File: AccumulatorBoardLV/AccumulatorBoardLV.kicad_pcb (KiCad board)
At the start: 4 copper layers, 152.4 x 50.8 mm, 50 parts, among them J1 Contactor 1, J10 To HV Board, J11 IMD Reset, J12 TS Interlock, J13 Temp Reset, J14 To ECU, J15 Charger LV, J16 Charger Interlock, J17 Lid Interlock, J18 From HV Board, J19 Chip 1, J2 BMS Connector 1, J20 Chip 2, J21 Chip 3, J22 Chip 4, J3 BMS Connector 2, J4 BMS TX, J5 BMS RX, J6 Current Sensor, J7 Contactor 2, J8 IMD LV, J9 BMS Reset, U1 DE1A1B-L2-12V, U10 MCP3008, U11 ISO1050, U12 stm_nucleo_FK303K8, U13 MCP3008, U14 MCP3008, U2 LM555N, U3 SN754410, U4 DE1A1B-L2-12V, U5 L78S05CV-DG, U6 DE1A1B-L2-12V, U7 DK1A1B-12V, U8 ADUM4154ARIZ, U9 MCP3008

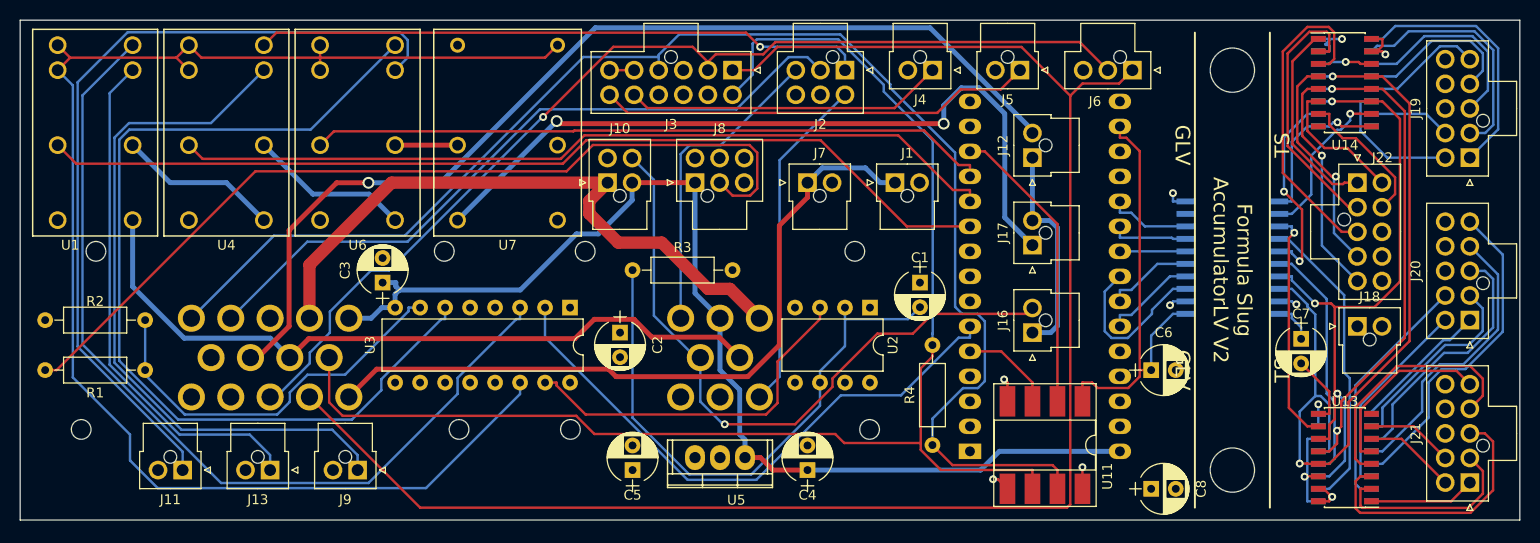
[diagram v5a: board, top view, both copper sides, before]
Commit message: Update DE relay footprint
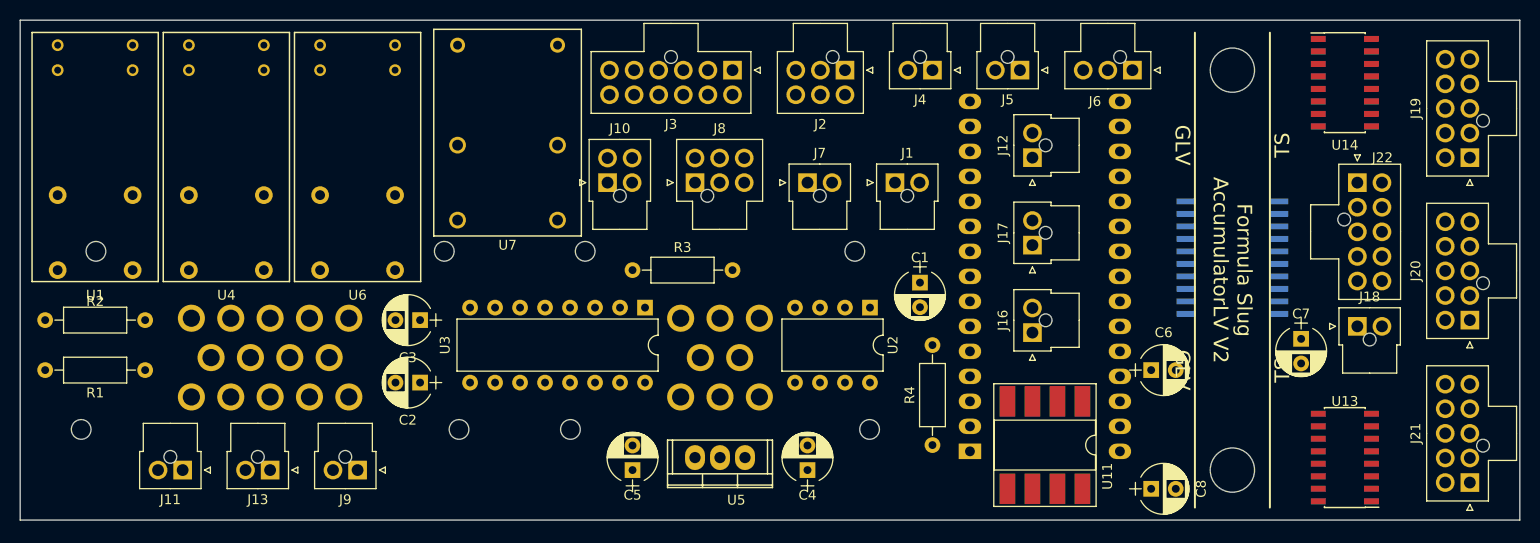
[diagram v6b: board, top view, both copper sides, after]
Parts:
- moved C2 20.9 mm to (80.9, 144.0), turned to 180 degrees
- moved U3 7.62 mm to (103.8, 136.4)
- moved C3 5.39 mm to (80.9, 137.7), turned to 180 degrees
- moved U1 5.08 mm to (44.1, 125.0)
- moved U4 5.08 mm to (57.4, 125.0)
- moved U6 5.08 mm to (70.7, 125.0)
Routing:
- net /5V_BMS: track 168.4 -> 0.00 mm
- net /TIMER_H: track 147.7 -> 0.00 mm
- net /CAN_H: track 146.8 -> 0.00 mm
- net /CAN_L: track 141.6 -> 0.00 mm
- net +12V: track 114.4 -> 0.00 mm
- net /SIG_CURRENT: track 105.2 -> 0.00 mm, vias 1 -> 0
- net /AIRS_ACC_OUT: track 103.7 -> 0.00 mm, vias 1 -> 0
- net /TEMP_FLT_LATCHED: track 98.1 -> 0.00 mm
- net /IMD_FLT_H: track 96.1 -> 0.00 mm
- net /TEMP_FLT_H: track 91.8 -> 0.00 mm
- net /IMD_FLT: track 90.5 -> 0.00 mm
- net /BMS_FLT_LATCHED: track 84.4 -> 0.00 mm
- net /IMD_RESET: track 83.4 -> 0.00 mm
- net /SCLK: track 81.8 -> 0.00 mm, vias 2 -> 0
- net /AIRS_RELAYS_OUT: track 78.1 -> 0.00 mm, vias 2 -> 0
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
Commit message: tweak boards slightly
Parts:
- added C9: CP, Capacitors_THT:C_Disc_D3.0mm_W1.6mm_P2.50mm, F.Cu at (145.7, 140.8)
- C2: value 0.47uF -> 0.1uF; footprint Capacitors_THT:CP_Radial_D5.0mm_P2.50mm -> Capacitors_THT:C_Disc_D3.0mm_W1.6mm_P2.50mm
- C3: value 10uF -> 0.1uF; footprint Capacitors_THT:CP_Radial_D5.0mm_P2.50mm -> Capacitors_THT:C_Disc_D3.0mm_W1.6mm_P2.50mm
- C6: value CP -> 0.1uF; footprint Capacitors_THT:CP_Radial_D5.0mm_P2.50mm -> Capacitors_THT:C_Disc_D3.0mm_W1.6mm_P2.50mm
- C7: value C -> 0.1uF; footprint Capacitors_THT:CP_Radial_D5.0mm_P2.50mm -> Capacitors_THT:C_Disc_D3.0mm_W1.6mm_P2.50mm
- C8: footprint Capacitors_THT:CP_Radial_D5.0mm_P2.50mm -> Capacitors_THT:C_Disc_D3.0mm_W1.6mm_P2.50mm
- moved R4 10.2 mm to (133.0, 140.2), turned to 270 degrees
- moved C8 9.71 mm to (145.7, 156.7), turned to 180 degrees
- moved C6 4.49 mm to (158.4, 139.6), turned to 180 degrees
- moved J16 2.54 mm to (143.1, 136.4)
- moved C7 1.91 mm to (168.5, 139.6), turned to 0 degrees
- moved J17 1.91 mm to (143.1, 128.1)
- moved C3 1.80 mm to (82.2, 136.4), turned to 270 degrees
- moved C2 1.27 mm to (82.2, 144.0), turned to 90 degrees
- moved J12 1.27 mm to (143.1, 119.9)
- moved U11 1.27 mm to (144.4, 149.1)
- moved U7 0.64 mm to (89.8, 119.3)
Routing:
- net /CAN_H: track 0.00 -> 136.6 mm
- net /CAN_L: track 0.00 -> 124.7 mm
- net /AIRS_ACC_OUT: track 0.00 -> 122.2 mm
- net /5V_BMS: track 0.00 -> 117.1 mm
- net /TIMER_H: track 0.00 -> 117.1 mm, vias 0 -> 1
- net /SIG_CURRENT: track 0.00 -> 116.7 mm, vias 0 -> 1
- net +12V: track 0.00 -> 116.5 mm, vias 0 -> 1
- net /TEMP_FLT_LATCHED: track 0.00 -> 101.6 mm, vias 0 -> 1
- net /IMD_FLT: track 0.00 -> 89.2 mm
- net /BMS_FLT_LATCHED: track 0.00 -> 88.3 mm, vias 0 -> 1
- net /AIRS_FINAL: track 0.00 -> 88.1 mm
- net /AIRS_RELAYS_OUT: track 0.00 -> 74.6 mm
- net /AIRS_FINAL_CHARGER: track 0.00 -> 74.2 mm
- net /TEMP_SSO: track 0.00 -> 73.1 mm, vias 0 -> 2
- net /V_L: track 0.00 -> 72.3 mm
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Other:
- net class Power: via_dia 2.4 -> 100

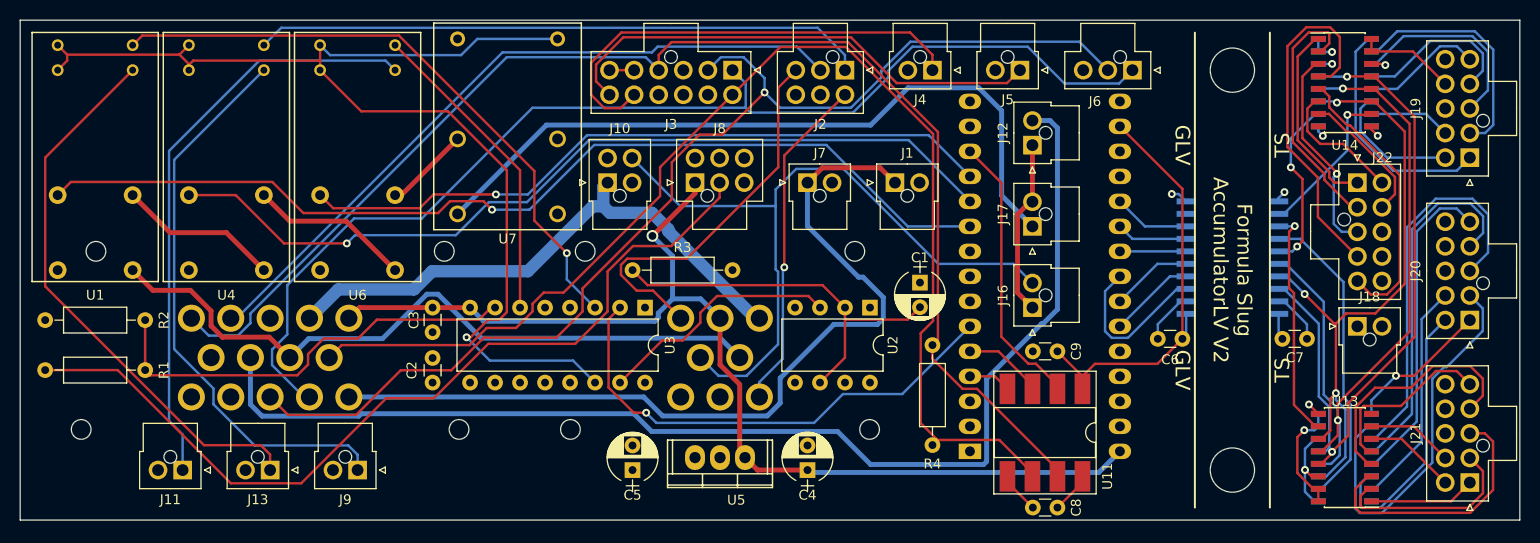
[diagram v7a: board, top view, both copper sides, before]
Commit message: add diodes to relay coils among other things
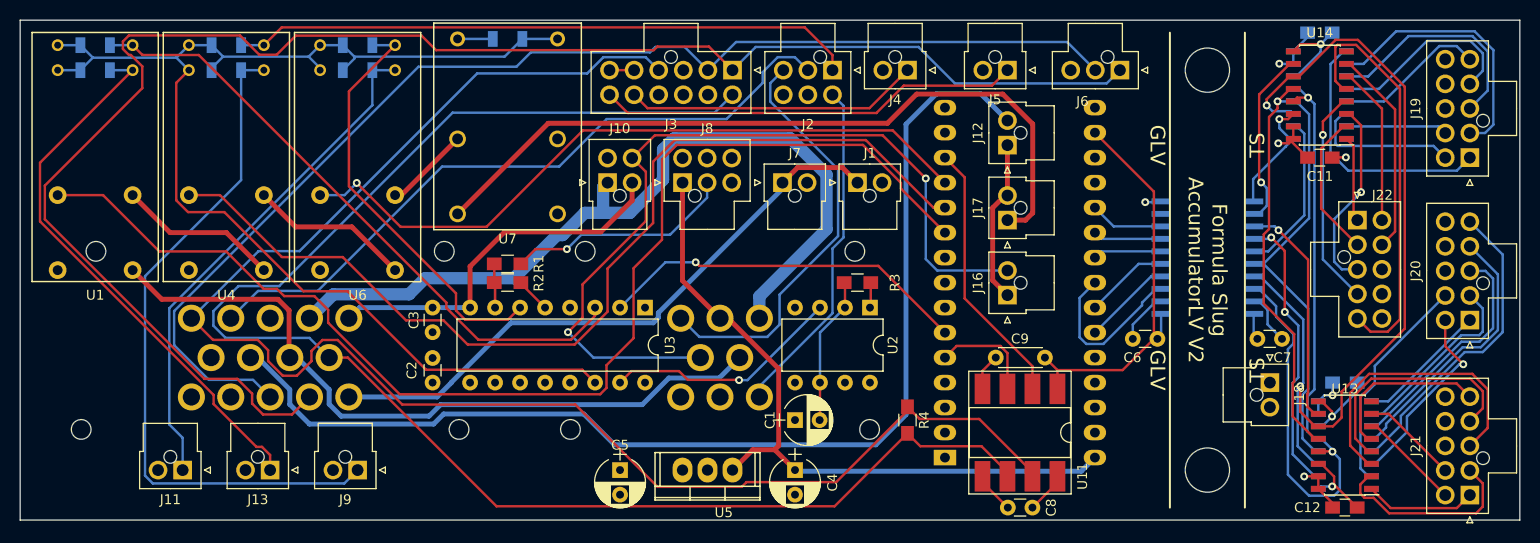
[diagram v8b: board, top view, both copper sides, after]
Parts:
- added C10: 1uF, Capacitors_SMD:C_0805_HandSoldering, B.Cu at (172.3, 108.5)
- added C11: 1uF, Capacitors_SMD:C_0805_HandSoldering, F.Cu at (172.3, 121.2)
- added C12: 1uF, Capacitors_SMD:C_0805_HandSoldering, F.Cu at (174.9, 156.7)
- added C13: 1uF, Capacitors_SMD:C_0805_HandSoldering, B.Cu at (174.9, 144.0)
- added D1: D, Diodes_SMD:D_1206, B.Cu at (47.9, 109.7)
- added D2: D, Diodes_SMD:D_1206, B.Cu at (47.9, 112.3)
- added D3: D, Diodes_SMD:D_1206, B.Cu at (61.2, 109.7)
- added D4: D, Diodes_SMD:D_1206, B.Cu at (61.2, 112.3)
- added D5: D, Diodes_SMD:D_1206, B.Cu at (74.5, 109.7)
- added D6: D, Diodes_SMD:D_1206, B.Cu at (74.5, 112.3)
- added D7: D, Diodes_SMD:D_1206, B.Cu at (89.8, 109.1)
- C9: footprint Capacitors_THT:C_Disc_D3.0mm_W1.6mm_P2.50mm -> Capacitors_THT:C_Disc_D4.3mm_W1.9mm_P5.00mm
- R1, R2, R3, R4: footprint Resistors_THT:R_Axial_DIN0207_L6.3mm_D2.5mm_P10.16mm_Horizontal -> Resistors_SMD:R_0805_HandSoldering
- moved R1 38.4 mm to (89.8, 132.0), turned to 0 degrees
- moved R2 37.0 mm to (89.8, 133.9), turned to 0 degrees
- moved R3 22.9 mm to (125.3, 133.9)
- moved C1 18.9 mm to (119.0, 147.8), turned to 0 degrees
- moved J18 10.6 mm to (167.3, 144.0), turned to 270 degrees
- moved R4 8.03 mm to (130.4, 147.8)
- moved J22 3.81 mm to (176.1, 127.5)
- moved J1 3.81 mm to (125.3, 123.7)
- moved J16 2.84 mm to (140.6, 135.1)
- moved U14 2.84 mm to (172.3, 114.8), turned to 180 degrees
- moved U9 2.84 mm to (172.3, 114.8)
- moved J17 2.62 mm to (140.6, 127.5)
- moved U12 2.62 mm to (141.9, 132.6)
- moved C8 2.54 mm to (143.1, 156.7)
- moved H1 2.54 mm to (160.9, 112.3)
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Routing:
- net /IMD_FLT: track 89.2 -> 23.2 mm, vias 0 -> 1
- net /5V_BMS: track 117.1 -> 167.5 mm
- net /IMD_FLT_5: track 44.3 -> 4.48 mm
- net /CAN_L: track 124.7 -> 156.8 mm
- net /12V_SRC: track 57.9 -> 84.1 mm
- net /CAN_H: track 136.6 -> 162.5 mm
- net /AIRS_FINAL: track 88.1 -> 62.6 mm
- net Net-(C1-Pad2): track 40.0 -> 15.1 mm
- net /TEMP_SSI: track 65.2 -> 89.1 mm, vias 3 -> 2
- net /TEMP_FLT_LATCHED: track 101.6 -> 124.1 mm, vias 1 -> 0
- net /BATT-: track 22.6 -> 45.2 mm, vias 7 -> 5
- net Net-(J20-Pad2): track 39.2 -> 19.0 mm
- net /BMS_TX: track 47.2 -> 29.9 mm
- net Net-(J20-Pad3): track 39.8 -> 24.2 mm
- net Net-(J22-Pad4): track 36.5 -> 22.2 mm, vias 0 -> 1
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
